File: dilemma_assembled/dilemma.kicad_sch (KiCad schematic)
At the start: 250 parts, among them J1 USB_C_Receptacle_USB2.0, J102 NA_serial, J105 NA_Conn_01x04_Female, J113 Cirque, J2 NA_Conn_01x03_Female, J3 NA_GC9A01, J4 Conn_01x05, J5 NA_Conn_01x02, J5001 USB_C_Receptacle_USB2.0, J5002 NA_Conn_01x02, J5003 NA_serial, J5004 NA_GC9A01, J5005 NA_Conn_01x04_Female, J5006 NA_Conn_01x03_Female, J5007 Cirque, J5008 Conn_01x05, J5009 Conn_01x05, J5010 Conn_01x05, SW1 SW_Push, SW101 NA_SW_Push, SW102 NA_SW_Push, SW103 NA_SW_Push, SW104 NA_SW_Push, SW105 NA_SW_Push, SW106 NA_SW_Push, SW107 NA_SW_Push, SW108 NA_SW_Push, SW109 NA_SW_Push, SW112 NA_SW_Push, SW113 NA_SW_Push, SW114 NA_SW_Push, SW115 NA_SW_Push, SW116 NA_SW_Push, SW117 NA_SW_Push, SW118 NA_SW_Push, SW119 NA_SW_Push, SW3001 NA_SW_Push, SW3002 NA_RotaryEncoder_Switch, SW5001 SW_Push, SW5002 NA_SW_Push, SW5003 NA_SW_Push, SW5004 NA_SW_Push, SW5005 NA_SW_Push, SW5006 NA_SW_Push, SW5007 NA_SW_Push, SW5008 NA_SW_Push, SW5009 NA_SW_Push, SW5010 NA_SW_Push, SW5011 NA_SW_Push, SW5012 NA_SW_Push, SW5013 NA_SW_Push, SW5014 NA_SW_Push, SW5015 NA_SW_Push, SW5016 NA_SW_Push, SW5017 NA_SW_Push, SW5018 NA_SW_Push, SW5019 NA_SW_Push, SW5020 NA_RotaryEncoder_Switch, SW5021 SW_SPST, SW5022 SW_SPST, U1 RP2040, U2 W25Q128JVS, U3 XC6210B332MR-G, U4 USBLC6-2P6, U5001 XC6210B332MR-G, U5002 RP2040, U5003 USBLC6-2P6, U5004 W25Q128JVS, Y1 Crystal_GND24, Y5001 Crystal_GND24

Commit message: add per key RGB
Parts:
- gave numbers to parts that had none: 19
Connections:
- net +3V3: now also D12.2 (VDD), D16.2 (VDD), D19.2 (VDD), D22.2 (VDD), D25.2 (VDD), D28.2 (VDD), D4.2 (VDD), D5.2 (VDD), D8.2 (VDD), D9.2 (VDD)
- net +3V3_L: now also D5014.2 (VDD), D5015.2 (VDD), D5017.2 (VDD), D5019.2 (VDD), D5021.2 (VDD), D5023.2 (VDD), D5025.2 (VDD), D5027.2 (VDD), D5029.2 (VDD), D5030.2 (VDD)

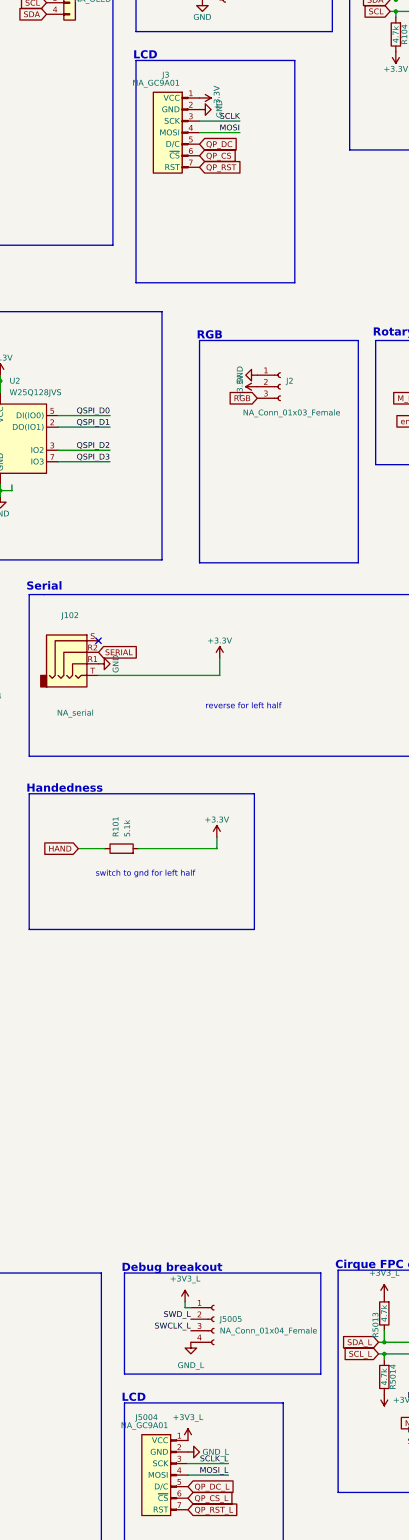
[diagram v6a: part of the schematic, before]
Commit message: switch vcc gnd on lcd
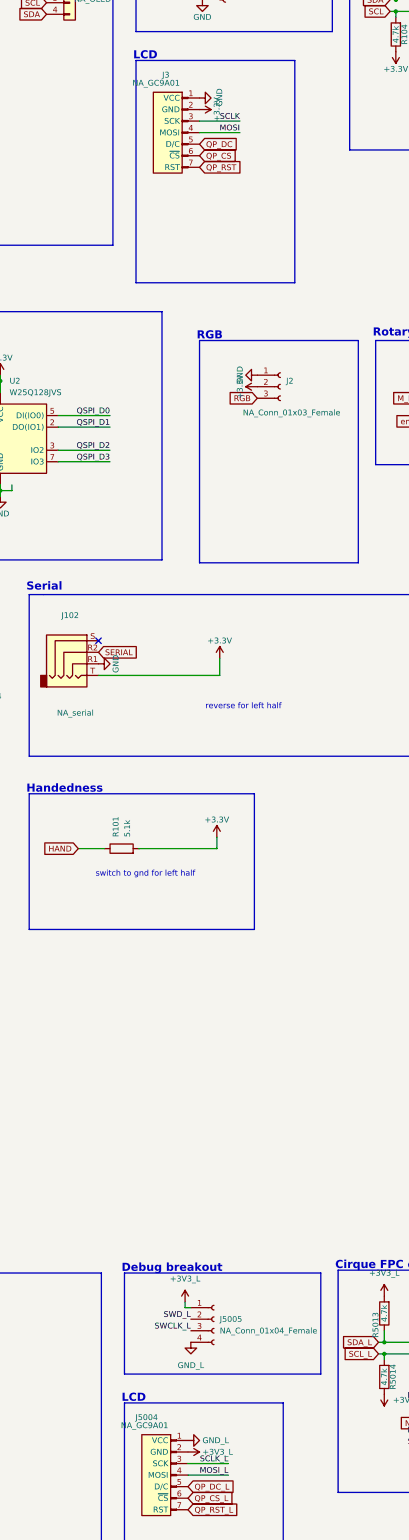
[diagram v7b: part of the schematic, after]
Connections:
- net +3V3: now also J3.2 (GND); no longer J3.1 (VCC)
- net +3V3_L: now also J5004.2 (GND); no longer J5004.1 (VCC)
- net GND: now also J3.1 (VCC); no longer J3.2 (GND)
- net GND_L: now also J5004.1 (VCC); no longer J5004.2 (GND)
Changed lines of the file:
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@@
     (pin "2")
   )
-  (symbol (lib_id "power_L:+3V3_L") (at 285.115 352.425 0) (unit 1)
+  (symbol (lib_id "power_L:+3V3_L") (at 285.115 354.965 270) (unit 1)
     (in_bom yes) (on_board yes) (fields_autoplaced)
-    (property "Reference" "#PWR05043" (id 0) (at 285.115 356.235 0)
+    (property "Reference" "#PWR05043" (id 0) (at 281.305 354.965 0)
       (effects (font (size 1.27 1.27)) hide)
     )
-    (property "Value" "+3V3_L" (id 1) (at 285.115 347.345 0))
-    (property "Footprint" "" (id 2) (at 285.115 352.425 0)
+    (property "Value" "+3V3_L" (id 1) (at 288.29 354.9649 90)
+      (effects (font (size 1.27 1.27)) (justify left))
+    )
+    (property "Footprint" "" (id 2) (at 285.115 354.965 0)
       (effects (font (size 1.27 1.27)) hide)
     )
-    (property "Datasheet" "" (id 3) (at 285.115 352.425 0)
+    (property "Datasheet" "" (id 3) (at 285.115 354.965 0)
       (effects (font (size 1.27 1.27)) hide)
     )
@@
     (pin "7")
   )
-  (symbol (lib_id "power:+3.3V") (at 287.655 57.15 270) (unit 1)
+  (symbol (lib_id "power:+3.3V") (at 287.655 59.69 270) (unit 1)
     (in_bom yes) (on_board yes)
-    (property "Reference" "#PWR0109" (id 0) (at 283.845 57.15 0)
+    (property "Reference" "#PWR0109" (id 0) (at 283.845 59.69 0)
       (effects (font (size 1.27 1.27)) hide)
     )
-    (property "Value" "+3.3V" (id 1) (at 291.465 57.15 0))
-    (property "Footprint" "" (id 2) (at 287.655 57.15 0)
+    (property "Value" "+3.3V" (id 1) (at 291.465 59.69 0))
+    (property "Footprint" "" (id 2) (at 287.655 59.69 0)
       (effects (font (size 1.27 1.27)) hide)
     )
-    (property "Datasheet" "" (id 3) (at 287.655 57.15 0)
+    (property "Datasheet" "" (id 3) (at 287.655 59.69 0)
       (effects (font (size 1.27 1.27)) hide)
     )
@@
     (pin "1")
   )
-  (symbol (lib_id "power_L:GND_L") (at 285.115 354.965 90) (unit 1)
+  (symbol (lib_id "power_L:GND_L") (at 285.115 352.425 90) (unit 1)
     (in_bom yes) (on_board yes) (fields_autoplaced)
-    (property "Reference" "#PWR05044" (id 0) (at 291.465 354.965 0)
+    (property "Reference" "#PWR05044" (id 0) (at 291.465 352.425 0)
       (effects (font (size 1.27 1.27)) hide)
     )
-    (property "Value" "GND_L" (id 1) (at 288.29 354.9649 90)
+    (property "Value" "GND_L" (id 1) (at 288.29 352.4249 90)
       (effects (font (size 1.27 1.27)) (justify right))
     )
-    (property "Footprint" "" (id 2) (at 285.115 354.965 0)
+    (property "Footprint" "" (id 2) (at 285.115 352.425 0)
       (effects (font (size 1.27 1.27)) hide)
     )
-    (property "Datasheet" "" (id 3) (at 285.115 354.965 0)
+    (property "Datasheet" "" (id 3) (at 285.115 352.425 0)
       (effects (font (size 1.27 1.27)) hide)
     )
@@
     (pin "5")
   )
-  (symbol (lib_id "power:GND") (at 287.655 59.69 90) (unit 1)
+  (symbol (lib_id "power:GND") (at 287.655 57.15 90) (unit 1)
     (in_bom yes) (on_board yes)
-    (property "Reference" "#PWR0106" (id 0) (at 294.005 59.69 0)
+    (property "Reference" "#PWR0106" (id 0) (at 294.005 57.15 0)
       (effects (font (size 1.27 1.27)) hide)
     )
-    (property "Value" "GND" (id 1) (at 292.0492 59.563 0))
-    (property "Footprint" "" (id 2) (at 287.655 59.69 0)
+    (property "Value" "GND" (id 1) (at 292.0492 57.023 0))
+    (property "Footprint" "" (id 2) (at 287.655 57.15 0)
       (effects (font (size 1.27 1.27)) hide)
     )
-    (property "Datasheet" "" (id 3) (at 287.655 59.69 0)
+    (property "Datasheet" "" (id 3) (at 287.655 57.15 0)
       (effects (font (size 1.27 1.27)) hide)
     )

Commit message: update BOM
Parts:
- R5015, R5016: value 1k -> 330
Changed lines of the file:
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@@
     (in_bom yes) (on_board yes)
     (property "Reference" "R5016" (id 0) (at 382.27 31.75 90))
-    (property "Value" "1k" (id 1) (at 382.27 34.29 90))
+    (property "Value" "330" (id 1) (at 382.27 34.29 90))
     (property "Footprint" "Resistor_SMD:R_0402_1005Metric" (id 2) (at 382.27 36.068 90)
       (effects (font (size 1.27 1.27)) hide)
@@
     (in_bom yes) (on_board yes)
     (property "Reference" "R5015" (id 0) (at 381 327.66 90))
-    (property "Value" "1k" (id 1) (at 381 330.2 90))
+    (property "Value" "330" (id 1) (at 381 330.2 90))
     (property "Footprint" "Resistor_SMD:R_0402_1005Metric" (id 2) (at 381 331.978 90)
       (effects (font (size 1.27 1.27)) hide)
@@
     )
     (path "/8c86a2ff-7652-4582-8eba-01bc6ccde085"
-      (reference "R5015") (unit 1) (value "1k") (footprint "Resistor_SMD:R_0402_1005Metric")
+      (reference "R5015") (unit 1) (value "330") (footprint "Resistor_SMD:R_0402_1005Metric")
     )
     (path "/584e719d-84f8-4d1d-8c33-91e89c98c372"
-      (reference "R5016") (unit 1) (value "1k") (footprint "Resistor_SMD:R_0402_1005Metric")
+      (reference "R5016") (unit 1) (value "330") (footprint "Resistor_SMD:R_0402_1005Metric")
     )
     (path "/c30a3276-ac5c-4a68-880e-26478e1b53e4"
